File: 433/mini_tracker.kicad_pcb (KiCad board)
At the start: 2 copper layers, 16 x 48 mm, 75 parts, among them J1 Conn_Coaxial, J2 Conn_01x05_Male, SW1 SW_DIP_x03, U1 SX1262, U2 AP2210N-3.3TRG1, U3 STM32G030F6P6, U4 SIM28ML, U5 SKY13453-385LF, Y1 NX2016SA-32MHZ-STD-CZS-5, Y2 NX2016SA-32MHZ-STD-CZS-5

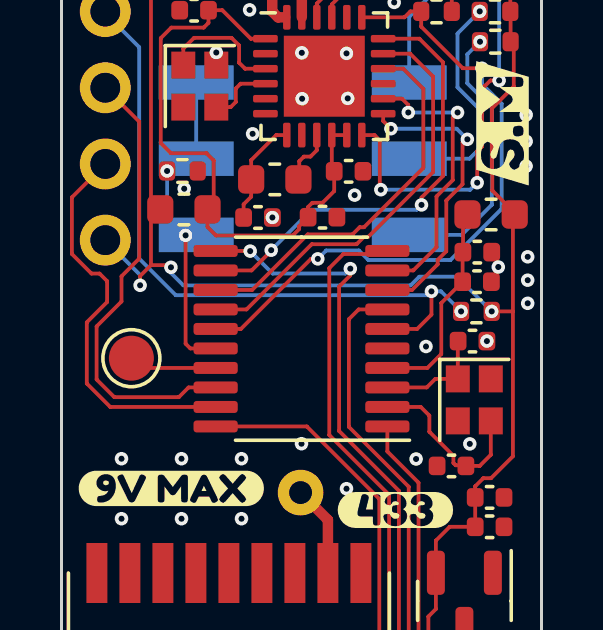
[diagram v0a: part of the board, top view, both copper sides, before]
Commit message: Update production files
-Fixed sta and pps label swap for both versions
-Completely redesign passive network for 868 version for lower extended components fee
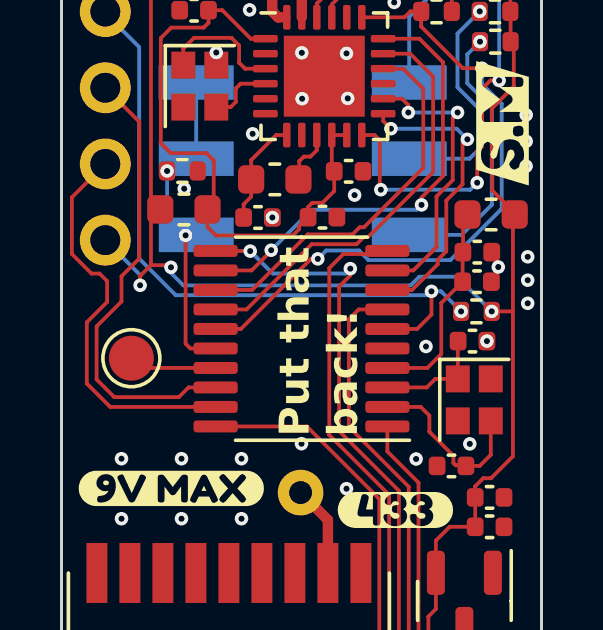
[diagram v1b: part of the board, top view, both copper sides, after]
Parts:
- removed kibuzzard-651ADEA2: G***, kibuzzard-651ADEA2
- removed kibuzzard-651ADEAE: G***, kibuzzard-651ADEAE
- added kibuzzard-65ED9408: G***, kibuzzard-65ED9408, B.Cu at (149.7, 122.0)
- added kibuzzard-65ED941B: G***, kibuzzard-65ED941B, B.Cu at (154.6, 122.0)
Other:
- board text added: "Put that back!"
